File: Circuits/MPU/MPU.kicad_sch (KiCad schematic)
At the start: 13 parts, among them J1 5-1814400-1, J10 Conn_02x10_Odd_Even, J11 Conn_02x25_Odd_Even, J13 MDM15_Plug, J2 5-1814400-1, J3 MDM9_Plug, J4 MDM9_Plug, J5 0010085031, J6 DE9_Receptacle, J7 MDM9_Receptacle, J8 Conn_02x05_Odd_Even, J9 Conn_02x13_Odd_Even, U1 ProASIC

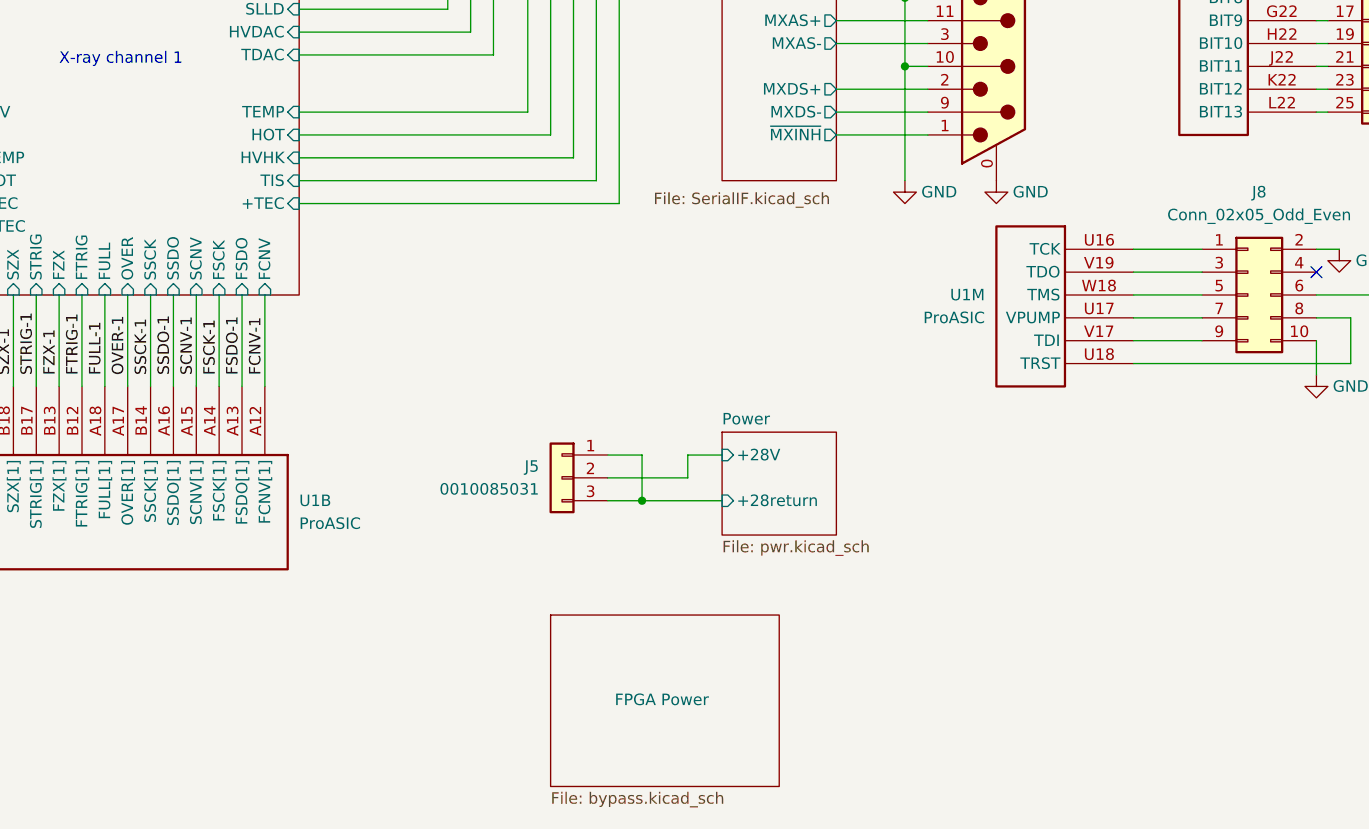
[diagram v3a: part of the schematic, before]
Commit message: Fix errors found by Norm Dobson
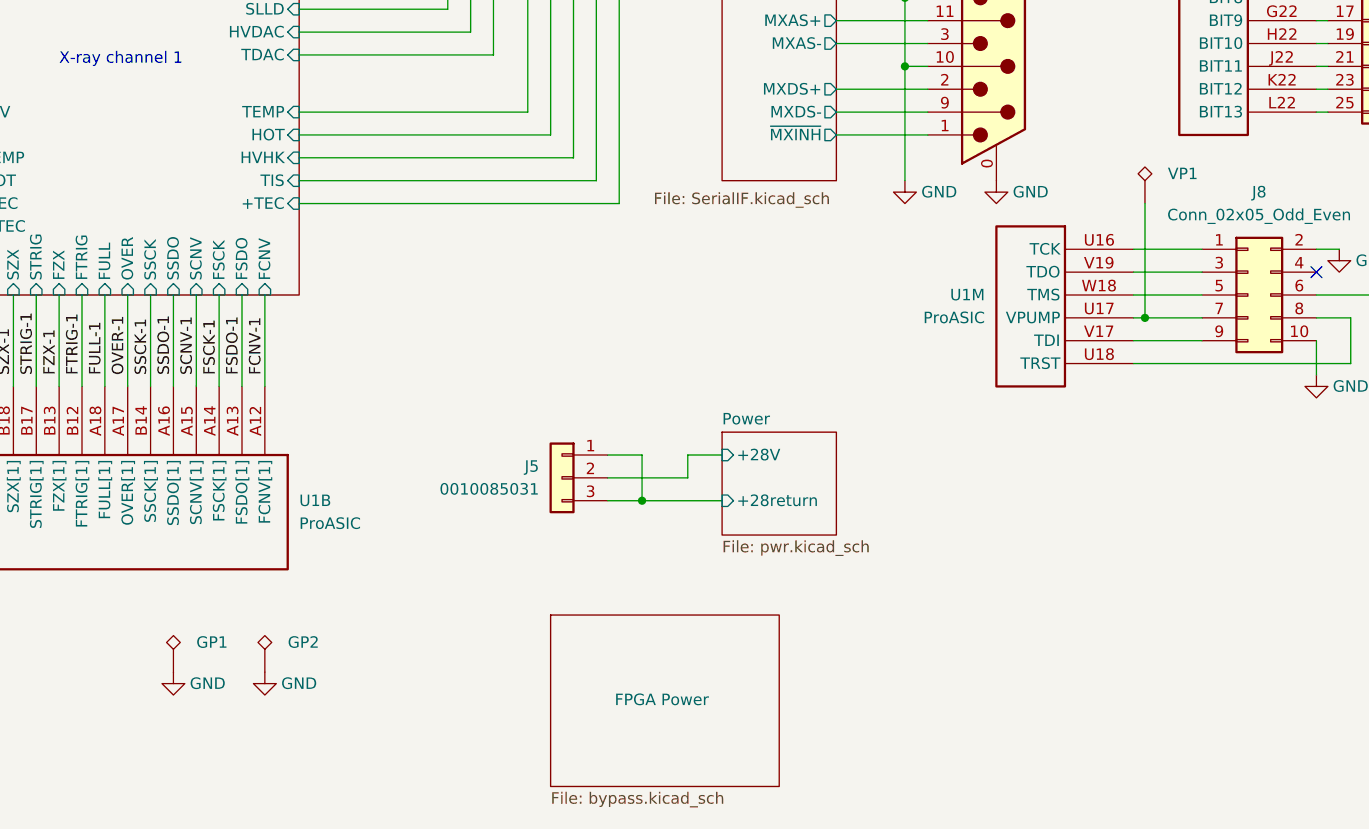
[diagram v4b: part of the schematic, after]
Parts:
- added GP1, GP2, VP1: TestPoint_Alt, TestPoint:TestPoint_Keystone_5015_Micro-Minature, symbol QuERI_symbols:TestPoint_Alt
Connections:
- net GND: now also GP1.1, GP2.1
- net at J8.7 (Pin_7), U1.U17 (VPUMP): now also VP1.1
